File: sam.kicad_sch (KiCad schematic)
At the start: 46 parts, among them IC1 4164, IC10 74ACT138, IC15 MC6883, IC16 74LS244N, IC2 4164, IC3 4164, IC31 74LS02N, IC33 74ACT138N, IC36 74LS132, IC37 GAL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

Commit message: redo layout for SAMx8
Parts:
- C10, C12: footprint Capacitor_THT:C_Rect_L7.0mm_W2.5mm_P5.00mm -> PCM_Capacitor_SMD_AKL:C_0805_2012Metric_Pad1.18x1.45mm_HandSolder
- C40: footprint Capacitor_THT:C_Disc_D3.0mm_W2.0mm_P2.50mm -> PCM_Capacitor_SMD_AKL:C_0603_1608Metric_Pad1.08x0.95mm_HandSolder; DigiKey 399-13930-1-ND -> (none)
- C41: footprint Capacitor_THT:C_Disc_D3.0mm_W2.0mm_P2.50mm -> PCM_Capacitor_SMD_AKL:C_0603_1608Metric_Pad1.08x0.95mm_HandSolder; DigiKey BC1007CT-ND -> (none)
- R12: footprint Resistor_THT:R_Axial_DIN0207_L6.3mm_D2.5mm_P2.54mm_Vertical -> PCM_Resistor_SMD_AKL:R_0805_2012Metric_Pad1.20x1.40mm_HandSolder
- R19, R20, R21, R22, R23, R24, R25, R26, R27, R28, R66: footprint Resistor_THT:R_Axial_DIN0207_L6.3mm_D2.5mm_P2.54mm_Vertical -> PCM_Resistor_SMD_AKL:R_0805_2012Metric_Pad1.20x1.40mm_HandSolder; DigiKey CF14JT22R0CT-ND -> (none)
- R37: footprint Resistor_THT:R_Axial_DIN0207_L6.3mm_D2.5mm_P10.16mm_Horizontal -> PCM_Resistor_SMD_AKL:R_0603_1608Metric_Pad1.05x0.95mm_HandSolder; DigiKey CF14JT1K50CT-ND -> (none)
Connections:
- net RAM VCC is gone; now on net Z7: IC1.9 (VCC), IC2.9 (VCC), IC3.9 (VCC), IC4.9 (VCC), IC5.9 (VCC), IC6.9 (VCC), IC7.9 (VCC), IC8.9 (VCC), R12.1
- net Z7: no longer IC15.35 (Z7(~{RAS1})), R12.2
- net ~{RAS0}: no longer IC36.1, IC36.2
- net ~{RAS}: now reaches IC15.12 (~{RAS0}), R26.2
- net ~{RAS}: now also IC36.1, IC36.2
- new net: IC15.35 (Z7(~{RAS1})), R12.2
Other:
- moved on the sheet: IC36A, IC36B, IC36C, R12, R26, R66

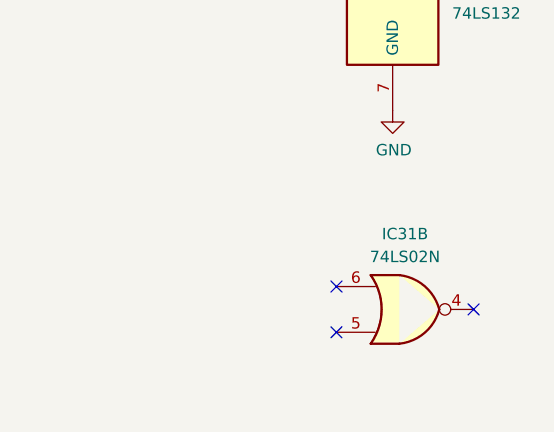
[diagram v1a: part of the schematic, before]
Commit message: add uart to board
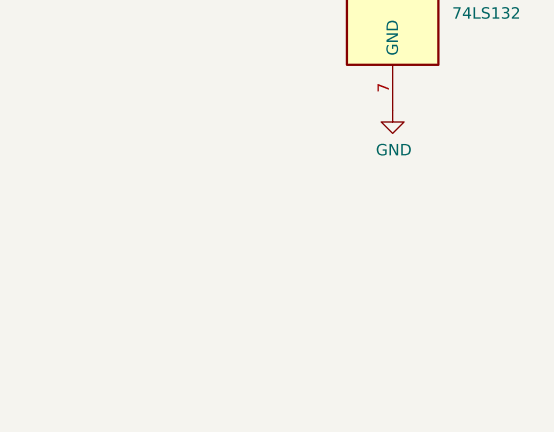
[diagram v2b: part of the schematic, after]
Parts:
- removed unit 2 of IC31
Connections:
- no-connect marks 10 -> 7
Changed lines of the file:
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@@
 	)
 	(no_connect
-		(at 394.8176 241.808)
-	)
-	(no_connect
 		(at 259.842 179.832)
 	)
@@
 	)
 	(no_connect
-		(at 379.5776 244.348)
-	)
-	(no_connect
-		(at 379.5776 239.268)
-	)
-	(no_connect
 		(at 259.842 184.912)
 	)
@@
 				)
 			)
-		)
-	)
-	(symbol
-		(lib_id "74xx:74LS02")
-		(at 387.1976 241.808 0)
-		(mirror x)
-		(unit 2)
-		(exclude_from_sim no)
-		(in_bom yes)
-		(on_board yes)
-		(dnp no)
-		(fields_autoplaced yes)
-		(property "Reference" "IC31"
-			(at 387.1976 233.426 0)
-			(effects
-				(font
-					(size 1.27 1.27)
-				)
-			)
-		)
-		(property "Value" "74LS02N"
-			(at 387.1976 235.966 0)
-			(effects
-				(font
-					(size 1.27 1.27)
-				)
-			)
-		)
-		(property "Footprint" "Package_DIP:DIP-14_W7.62mm"
-			(at 387.1976 241.808 0)
-			(effects
-				(font
-					(size 1.27 1.27)
-				)
-				(hide yes)
-			)
-		)
-		(property "Datasheet" "http://www.ti.com/lit/gpn/sn74ls02"
-			(at 387.1976 241.808 0)
-			(effects
-				(font
-					(size 1.27 1.27)
-				)
-				(hide yes)
-			)
-		)
-		(property "Description" ""
-			(at 387.1976 241.808 0)
-			(effects
-				(font
-					(size 1.27 1.27)
-				)
-				(hide yes)
-			)
-		)
-		(property "DigiKey" "296-1627-5-ND"
-			(at 387.1976 241.808 0)
-			(effects
-				(font
-					(size 1.27 1.27)
-				)
-				(hide yes)
-			)
-		)
-		(property "SA2120" "Sheet 1 (spare)"
-			(at 387.1976 241.808 0)
-			(effects
-				(font
-					(size 1.27 1.27)
-				)
-				(hide yes)
-			)
-		)
-		(pin "1"
-		)
-		(pin "2"
-		)
-		(pin "3"
-		)
-		(pin "4"
-		)
-		(pin "5"
-		)
-		(pin "6"
-		)
-		(pin "10"
-		)
-		(pin "8"
-		)
-		(pin "9"
-		)
-		(pin "11"
-		)
-		(pin "12"
-		)
-		(pin "13"
-		)
-		(pin "14"
-		)
-		(pin "7"
-		)
-		(instances
-			(project "Dragon32"
-				(path "/0c3dceba-7c95-4b3d-b590-0eb581444beb/c0eaba02-6b8d-4a7f-b51d-5746c573781a"
-					(reference "IC31")
-					(unit 2)
-				)
-			)

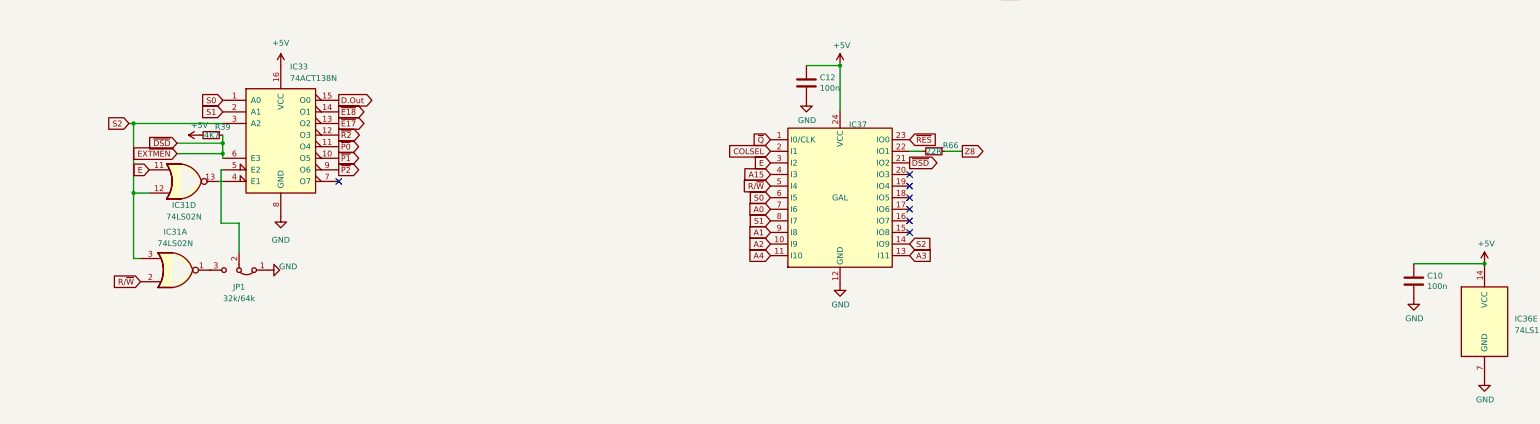
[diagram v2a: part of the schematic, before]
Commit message: update to keyboard switch option
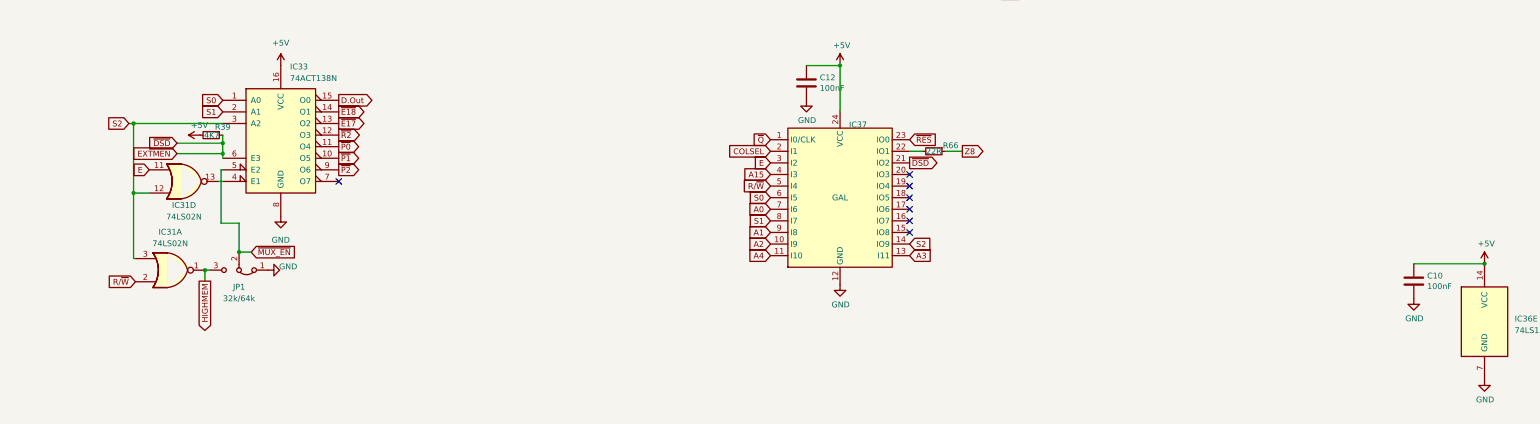
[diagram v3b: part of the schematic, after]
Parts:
- C10, C12: value 100n -> 100nF; LCSC (none) -> C1711
- C40: LCSC (none) -> C1653
- C41: LCSC (none) -> C1663
- IC1, IC15, IC2, IC3, IC33, IC4, IC5, IC6, IC7, IC8: SA2120 Sheet 1 -> (none)
- IC10: LCSC (none) -> C1547282
- IC16: LCSC (none) -> C22374098; SA2120 Sheet 1 -> (none)
- IC31: LCSC (none) -> C22374091; SA2120 Sheet 1 (spare) -> (none)
- R12: DigiKey CF14JT22R0CT-ND -> (none); LCSC (none) -> C17561
- R19, R20, R21, R22, R23, R24, R25, R26, R27, R28, R66: LCSC (none) -> C17561
- R37: LCSC (none) -> C22843
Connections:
- net ~{MUX_EN}: now reaches IC33.5 (E2), JP1.2 (C)
- net HIGHMEM: now reaches IC31.1, JP1.3 (B)
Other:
- title: (none) -> Dragon CPU UK Revised
- moved on the sheet: IC31A
